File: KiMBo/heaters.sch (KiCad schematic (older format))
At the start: 30 parts

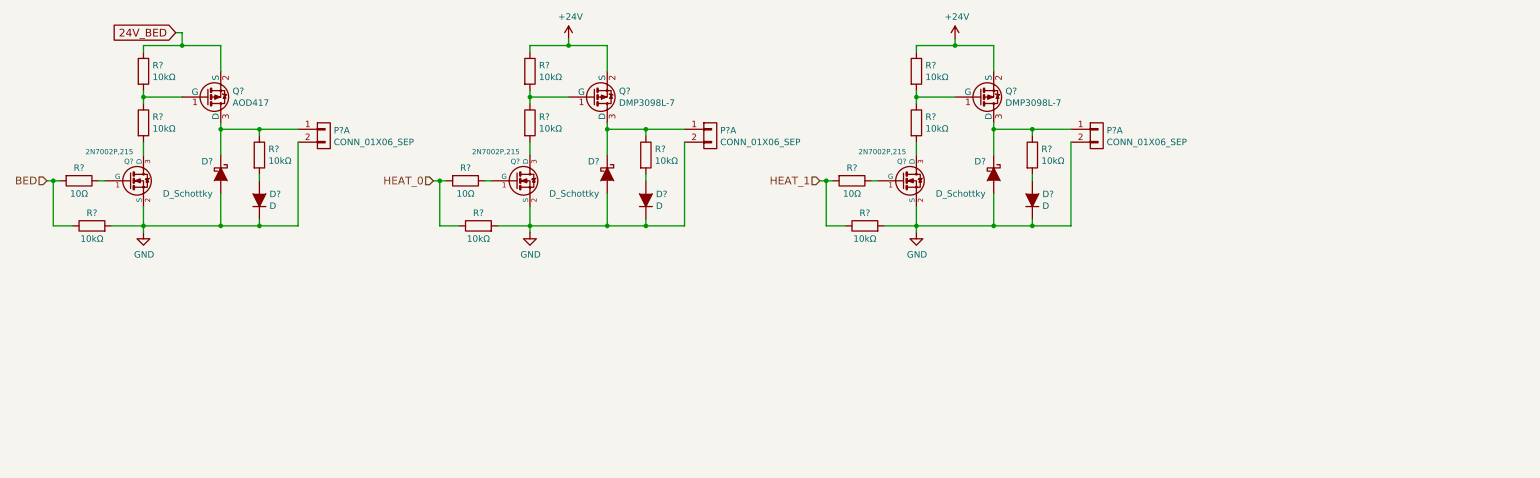
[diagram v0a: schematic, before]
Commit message: Add eMMC to the schematic
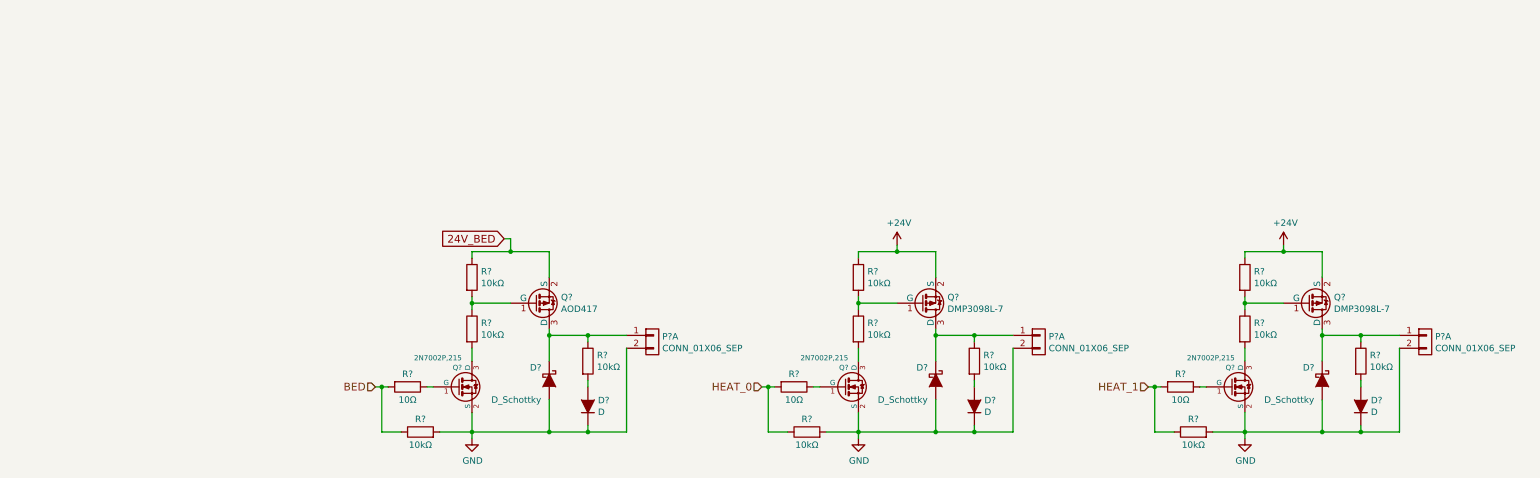
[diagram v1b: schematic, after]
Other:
- moved on the sheet: D?, P?A, Q?, R?
